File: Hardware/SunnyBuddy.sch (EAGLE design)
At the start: 33 parts, among them J1 5.5x2.1mm Barrel, J3 POWER_JACKPTH, J5 M02PTH, J6 M023.5MM, J7 M023.5MM, J8 M023.5MM, U1 LT3652

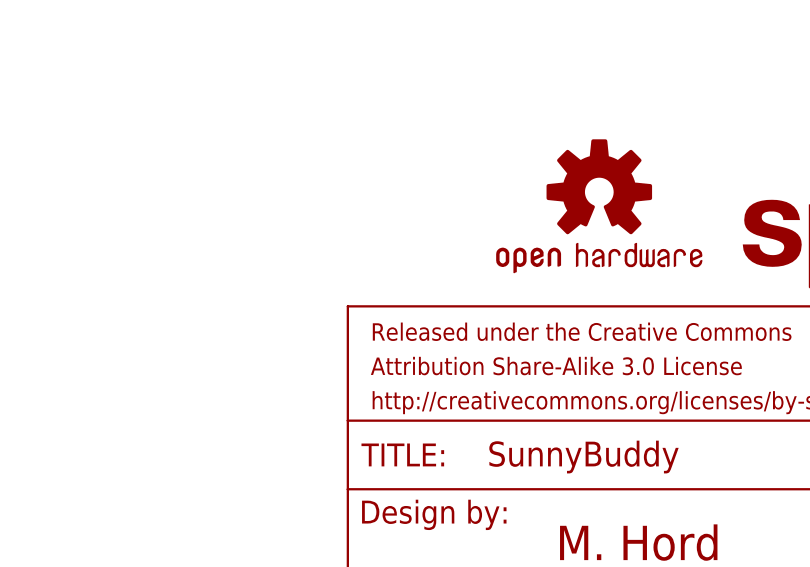
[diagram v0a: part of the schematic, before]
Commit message: Added local board fiducials
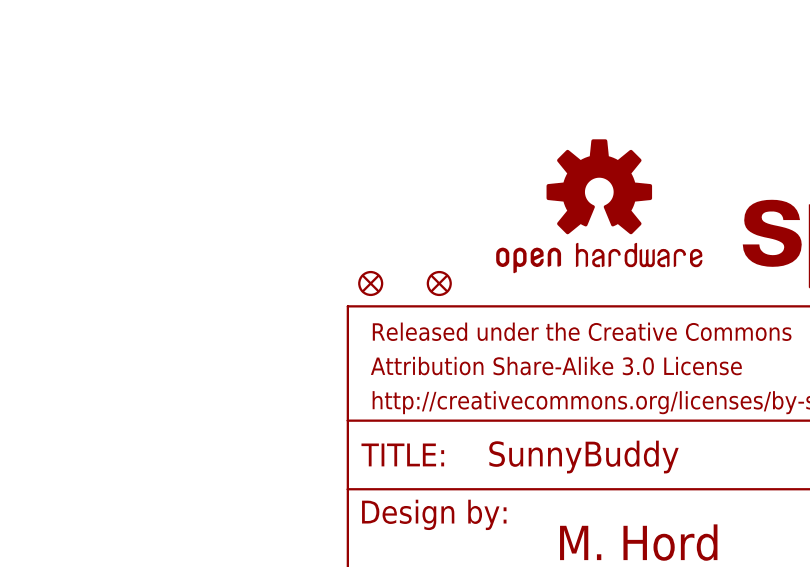
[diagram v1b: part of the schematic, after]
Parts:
- added FID1, FID2: FIDUCIAL1X2, SparkFun-Aesthetics:FIDUCIAL1X2
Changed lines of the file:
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@@
 <?xml version="1.0" encoding="utf-8"?>
 <!DOCTYPE eagle SYSTEM "eagle.dtd">
-<eagle version="6.4">
+<eagle version="6.5.0">
 <drawing>
 <settings>
@@
 <part name="GND7" library="SparkFun-Aesthetics" deviceset="GND" device=""/>
 <part name="R6" library="SparkFun-Resistors" deviceset="0OHM1/10W5%(0603)" device="" value="0"/>
+<part name="FID1" library="SparkFun-Aesthetics" deviceset="FIDUCIAL" device="1X2"/>
+<part name="FID2" library="SparkFun-Aesthetics" deviceset="FIDUCIAL" device="1X2"/>
 </parts>
 <sheets>
@@
 <instance part="GND7" gate="1" x="231.14" y="132.08"/>
 <instance part="R6" gate="G$1" x="111.76" y="104.14"/>
+<instance part="FID1" gate="G$1" x="149.86" y="38.1"/>
+<instance part="FID2" gate="G$1" x="157.48" y="38.1"/>
 </instances>
 <busses>
